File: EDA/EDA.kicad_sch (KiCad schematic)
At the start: 38 parts, among them J2 Screw_Terminal_01x02, M1 Motor_Servo, U1 PMCF8316A1VRGFR, U2 LM2596S-5, U3 LM2678S-5

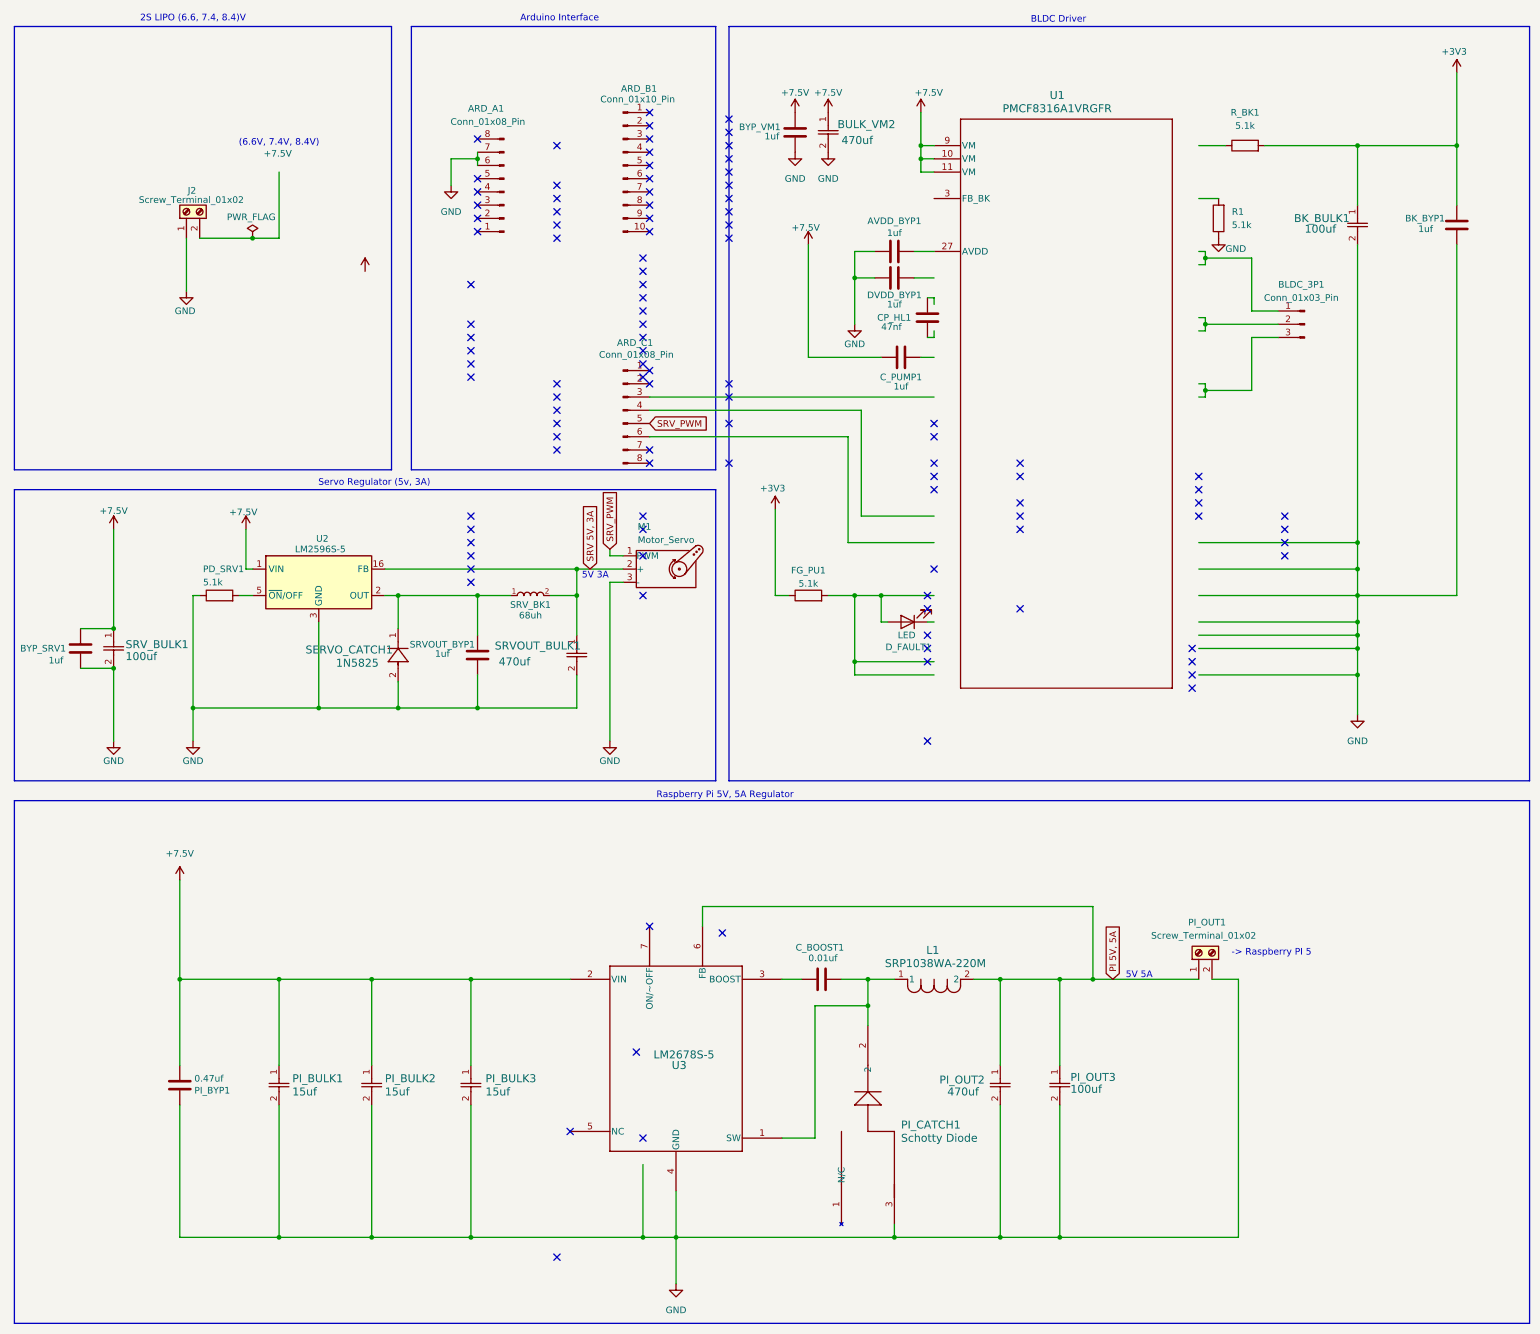
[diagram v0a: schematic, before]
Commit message: Started Routing PCB.
- Developed Pi 5V, 5A power supply.
- Working on 5V, 3A servo power supply.
- Yet to begin wiring BLDC motor controller logic.
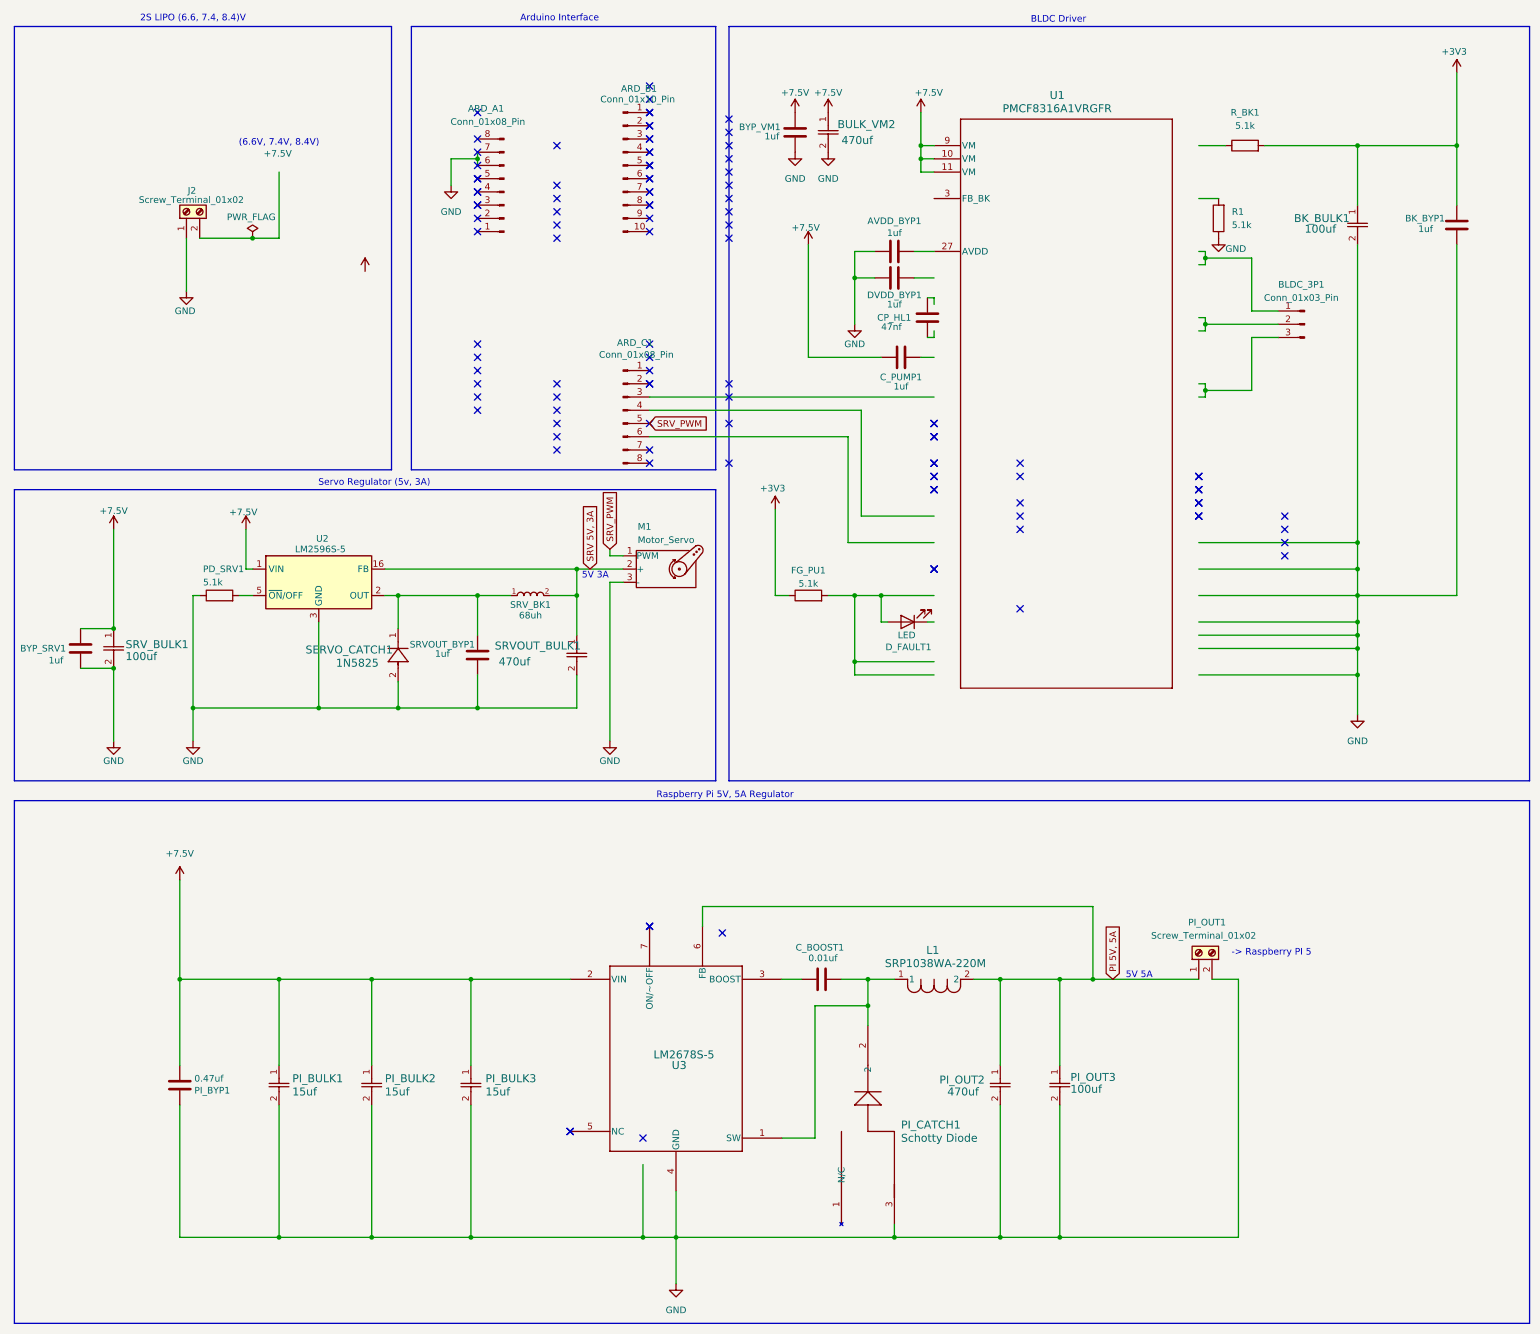
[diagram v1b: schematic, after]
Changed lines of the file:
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@@
 	)
 	(no_connect
-		(at 137.16 68.58)
+		(at 138.43 35.56)
 	)
 	(no_connect
-		(at 191.77 128.27)
+		(at 193.04 95.25)
 	)
 	(no_connect
-		(at 104.14 120.65)
+		(at 105.41 87.63)
 	)
 	(no_connect
-		(at 104.14 73.66)
+		(at 105.41 40.64)
 	)
 	(no_connect
-		(at 104.14 113.03)
+		(at 105.41 80.01)
 	)
 	(no_connect
-		(at 104.14 115.57)
+		(at 105.41 82.55)
 	)
 	(no_connect
-		(at 137.16 110.49)
+		(at 138.43 77.47)
 	)
 	(no_connect
-		(at 137.16 73.66)
+		(at 138.43 40.64)
 	)
 	(no_connect
-		(at 104.14 76.2)
+		(at 105.41 43.18)
 	)
 	(no_connect
-		(at 137.16 71.12)
+		(at 138.43 38.1)
 	)
 	(no_connect
-		(at 137.16 83.82)
+		(at 138.43 50.8)
 	)
 	(no_connect
-		(at 137.16 76.2)
+		(at 138.43 43.18)
 	)
 	(no_connect
-		(at 135.89 213.36)
+		(at 123.19 228.6)
 	)
 	(no_connect
-		(at 104.14 118.11)
+		(at 105.41 85.09)
 	)
 	(no_connect
-		(at 137.16 63.5)
+		(at 138.43 30.48)
 	)
 	(no_connect
-		(at 120.65 252.73)
+		(at 138.43 189.23)
 	)
 	(no_connect
-		(at 137.16 78.74)
+		(at 138.43 45.72)
 	)
 	(no_connect
-		(at 242.57 140.97)
+		(at 243.84 107.95)
 	)
 	(no_connect
-		(at 137.16 60.96)
+		(at 138.43 27.94)
 	)
 	(no_connect
-		(at 137.16 81.28)
+		(at 138.43 48.26)
 	)
 	(no_connect
-		(at 191.77 138.43)
+		(at 193.04 105.41)
 	)
 	(no_connect
-		(at 104.14 81.28)
+		(at 105.41 48.26)
 	)
 	(no_connect
-		(at 242.57 143.51)
+		(at 243.84 110.49)
 	)
 	(no_connect
-		(at 242.57 135.89)
+		(at 243.84 102.87)
 	)
 	(no_connect
-		(at 137.16 113.03)
+		(at 138.43 80.01)
 	)
 	(no_connect
-		(at 242.57 138.43)
+		(at 243.84 105.41)
 	)
 	(no_connect
-		(at 137.16 66.04)
+		(at 138.43 33.02)
 	)
 	(no_connect
-		(at 137.16 118.11)
+		(at 138.43 85.09)
 	)
 	(no_connect
-		(at 191.77 133.35)
+		(at 193.04 100.33)
 	)
 	(no_connect
-		(at 191.77 125.73)
+		(at 193.04 92.71)
 	)
 	(no_connect
-		(at 191.77 153.67)
+		(at 193.04 120.65)
 	)
 	(no_connect
-		(at 191.77 135.89)
+		(at 193.04 102.87)
 	)
 	(no_connect
-		(at 137.16 125.73)
+		(at 138.43 92.71)
 	)
 	(no_connect
-		(at 104.14 123.19)
+		(at 105.41 90.17)
 	)
 	(no_connect
-		(at 104.14 83.82)
+		(at 105.41 50.8)
 	)
 	(no_connect
-		(at 104.14 110.49)
+		(at 105.41 77.47)
 	)
 	(no_connect
-		(at 104.14 78.74)
+		(at 105.41 45.72)
 	)
 	(no_connect
-		(at 104.14 66.04)
+		(at 105.41 33.02)
 	)
 	(wire

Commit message: Add initial EDA project files and configuration
- Created EDA.step file for project steps.
- Added autosave configuration for EDA.kicad_prl with board settings, visibility options, and net inspector panel configurations.
- Introduced lock files for PCB and schematic with hostname and username information.
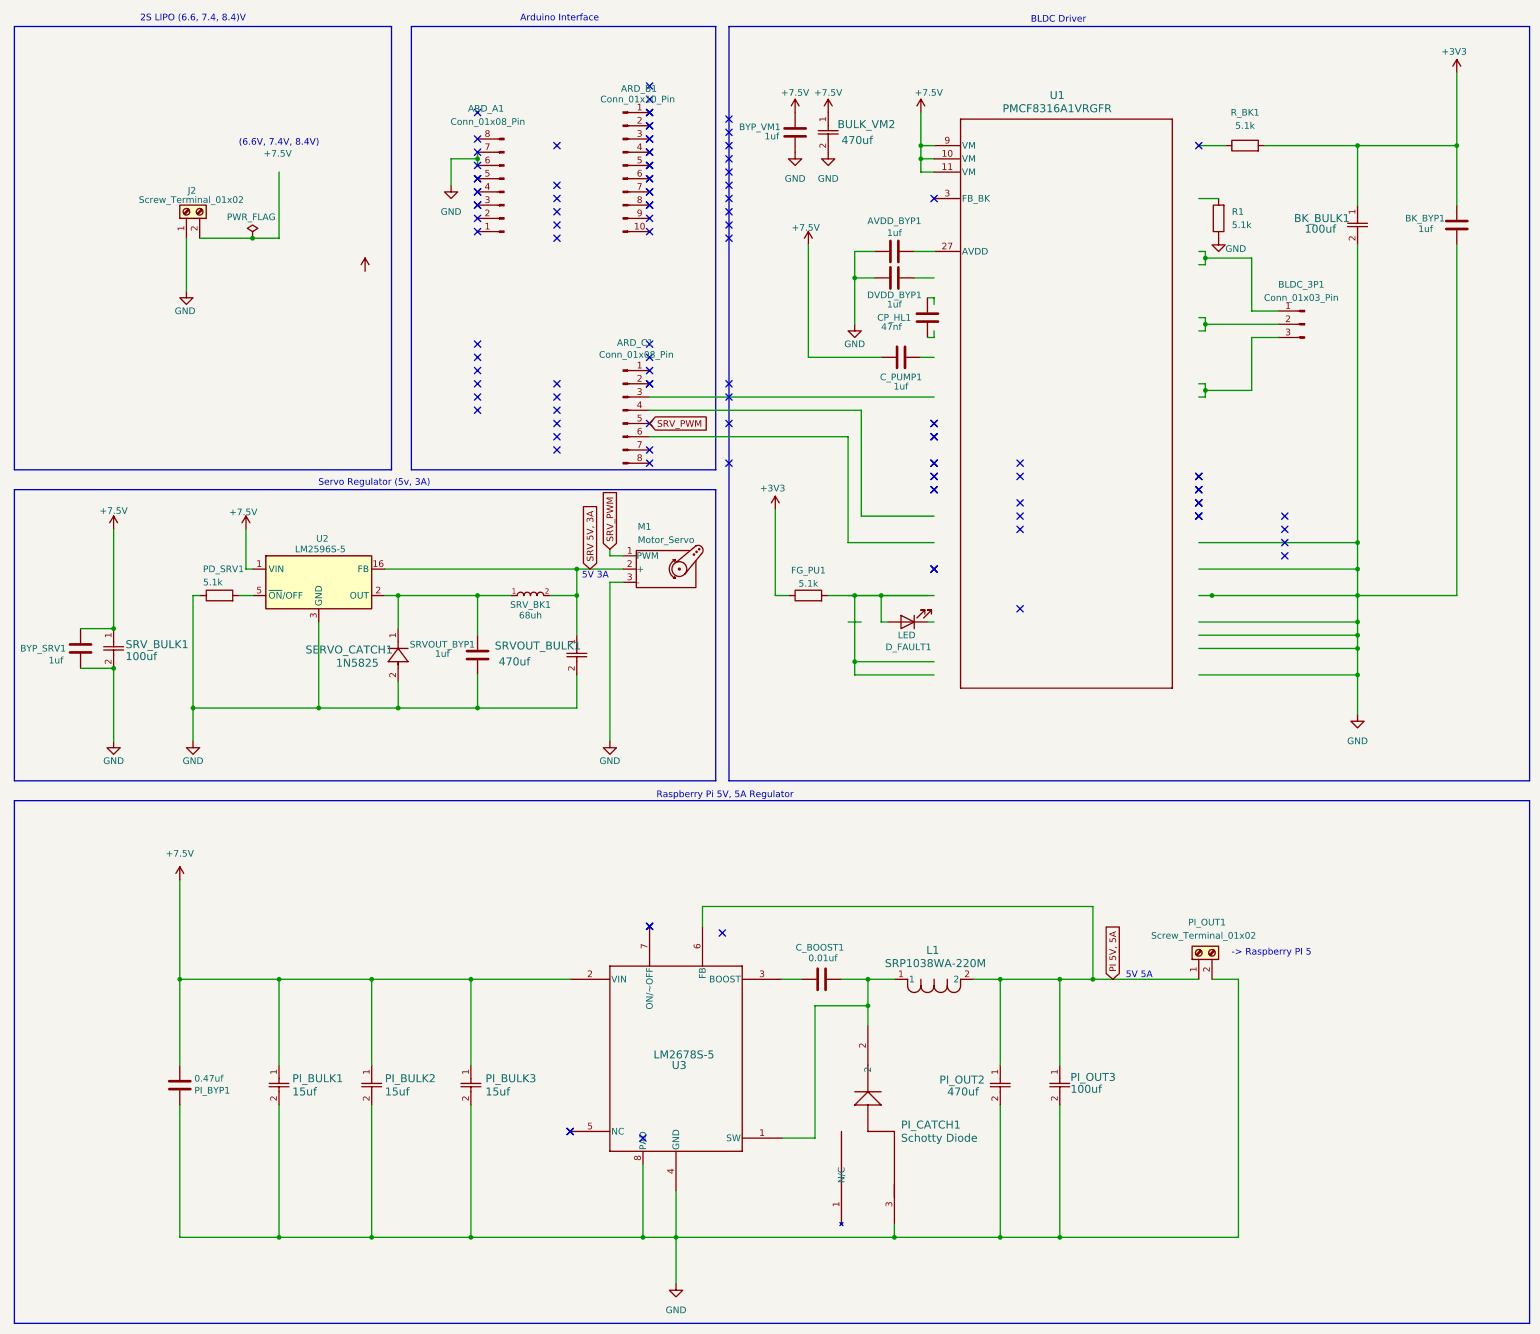
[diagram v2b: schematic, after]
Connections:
- net GND: now also U3.8 (PAD)
- no-connect marks 108 -> 110
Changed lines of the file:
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@@
+	)
+	(junction
+		(at 246.38 125.73)
+		(diameter 0)
+		(color 0 0 0 0)
 	)
 	(junction
@@
 	)
 	(no_connect
+		(at 193.04 49.53)
+	)
+	(no_connect
 		(at 138.43 40.64)
 	)
@@
 	)
 	(no_connect
+		(at 243.84 39.37)
+	)
+	(no_connect
 		(at 193.04 92.71)
 	)
@@
 	(wire
 		(pts
+			(xy 176.53 130.81) (xy 179.07 130.81)
+		)
+		(stroke
+			(width 0)
+			(type default)
+		)
+	)
+	(wire
+		(pts
 			(xy 190.5 33.02) (xy 190.5 39.37)
 		)
@@
 		)
 		(stroke
+			(width 0)
+			(type default)
+		)
+	)
+	(wire
+		(pts
+			(xy 176.53 125.73) (xy 191.77 125.73)
+		)
+		(stroke
